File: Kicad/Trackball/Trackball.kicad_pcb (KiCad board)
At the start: 2 copper layers, 231.1 x 134.1 mm, 52 parts, among them J1 Battery, J10 Conn_01x04_Female, J11 Conn_01x04_Female, J12 Conn_01x04_Female, J13 Conn_01x04_Female, J14 Conn_01x04_Female, J15 Conn_01x04_Female, J17 Conn_01x04_Female, J18 Conn_01x03_Pin, J19 Conn_01x03_Pin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

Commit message: B4: PCB outlines defined. To do: correct schematics - swap male/female sockets, move the buttons to appropriate PCBs. Add 44mm base and the bottom cover.
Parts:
- SW1, SW2, SW3: moved to F.Cu
- U1: moved to B.Cu
- moved H3 183.0 mm to (232.6, 101.6)
- moved H6 166.0 mm to (199.6, 82.5)
- moved H7 165.9 mm to (199.5, 120.7)
- moved MX4 149.3 mm to (245.0, 64.4), turned to 0 degrees
- moved MX1 149.2 mm to (245.0, 138.7)
- moved MX3 139.7 mm to (120.4, 139.5), turned to 180 degrees
- moved MX6 139.4 mm to (120.4, 64.4), turned to 0 degrees
- moved MX2 116.9 mm to (139.0, 139.5), turned to 180 degrees
- moved MX5 116.4 mm to (139.0, 64.4), turned to 0 degrees
- moved H4 107.0 mm to (221.6, 82.5)
- moved H5 106.9 mm to (221.5, 120.7)
- moved J17 82.0 mm to (73.9, 97.8)
- moved C1 76.8 mm to (28.4, 177.7)
- moved C2 76.8 mm to (29.5, 183.2)
- moved C3 76.8 mm to (29.3, 187.9)
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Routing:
- net Button4: track 61.0 -> 0.00 mm, vias 1 -> 0
- net Button5: track 60.0 -> 0.00 mm, vias 1 -> 0
- net Button6: track 58.9 -> 0.00 mm
- net MOTION: track 53.1 -> 0.00 mm, vias 1 -> 0
- net Button1: track 53.0 -> 0.00 mm, vias 1 -> 0
- net Button3: track 44.9 -> 0.00 mm
- net NCS: track 42.7 -> 0.00 mm, vias 1 -> 0
- net +3V3: track 40.9 -> 0.00 mm
- net SCLK: track 39.3 -> 0.00 mm
- net Net-(J1-Pin_2): track 39.2 -> 0.00 mm
- net Net-(J13-Pin_3): track 37.4 -> 0.00 mm, vias 1 -> 0
- net Button2: track 37.2 -> 0.00 mm, vias 1 -> 0
- net RST: track 35.9 -> 0.00 mm
- net BTReset: track 35.4 -> 0.00 mm
- net Net-(J10-Pin_3): track 34.0 -> 0.00 mm, vias 1 -> 0
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- removed copper zone on B.Cu, net GND_T
- removed copper zone on F.Cu, net GND_T
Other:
- board size 231.1 x 134.1 mm -> 238.4 x 138 mm
- board text added: "ThumbsUp! Trackball v4 44/52.5mm Ball"
- board text added: "u/ak66666 2025-09-19"
- board text added: "u/ak66666 ThumbsUp! Trackball v4 52.5mm Ball"
- board text removed: "ThumbsUp! Trackball v3"
- board text removed: "u/ak66666 2025-08-30"

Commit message: B4: Base,  Cover, 52.5 mm ball platform ready. TODO: add 44mm platform.
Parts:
- removed H2: MountingHole_Pad, MountingHole:MountingHole_2.5mm_Pad
- removed J11, J14, J17: Conn_01x04_Female, Connector_PinSocket_2.54mm:PinSocket_1x04_P2.54mm_Vertical
- removed J7, J8, J9: Conn_01x04_Male, Connector_PinHeader_2.54mm:PinHeader_1x04_P2.54mm_Vertical
- J1: moved to F.Cu
- J10: renamed from J2; value Conn_01x04_Male -> Conn_01x04_Female; footprint Connector_PinHeader_2.54mm:PinHeader_1x04_P2.54mm_Vertical -> Connector_PinSocket_2.54mm:PinSocket_1x04_P2.54mm_Vertical; moved to F.Cu
- J12: renamed from J5; value Conn_01x04_Male -> Conn_01x04_Female; footprint Connector_PinHeader_2.54mm:PinHeader_1x04_P2.54mm_Vertical -> Connector_PinSocket_2.54mm:PinSocket_1x04_P2.54mm_Vertical; moved to F.Cu
- J13: renamed from J3; value Conn_01x04_Male -> Conn_01x04_Female; footprint Connector_PinHeader_2.54mm:PinHeader_1x04_P2.54mm_Vertical -> Connector_PinSocket_2.54mm:PinSocket_1x04_P2.54mm_Vertical; moved to F.Cu
- J15: renamed from J4; value Conn_01x04_Male -> Conn_01x04_Female; footprint Connector_PinHeader_2.54mm:PinHeader_1x04_P2.54mm_Vertical -> Connector_PinSocket_2.54mm:PinSocket_1x04_P2.54mm_Vertical; moved to F.Cu
- J2: renamed from J10; value Conn_01x04_Female -> Conn_01x04_Male; footprint Connector_PinSocket_2.54mm:PinSocket_1x04_P2.54mm_Vertical -> Connector_PinHeader_2.54mm:PinHeader_1x04_P2.54mm_Vertical; moved to B.Cu
- J3: renamed from J13; value Conn_01x04_Female -> Conn_01x04_Male; footprint Connector_PinSocket_2.54mm:PinSocket_1x04_P2.54mm_Vertical -> Connector_PinHeader_2.54mm:PinHeader_1x04_P2.54mm_Vertical; moved to B.Cu
- J4: renamed from J15; value Conn_01x04_Female -> Conn_01x04_Male; footprint Connector_PinSocket_2.54mm:PinSocket_1x04_P2.54mm_Vertical -> Connector_PinHeader_2.54mm:PinHeader_1x04_P2.54mm_Vertical; moved to B.Cu
- J5: renamed from J12; value Conn_01x04_Female -> Conn_01x04_Male; footprint Connector_PinSocket_2.54mm:PinSocket_1x04_P2.54mm_Vertical -> Connector_PinHeader_2.54mm:PinHeader_1x04_P2.54mm_Vertical; moved to B.Cu
- moved J1 72.8 mm to (140.7, 89.1), turned to -135 degrees
- moved BT_RESET1 37.2 mm to (163.2, 68.1), turned to 90 degrees
- moved STUDIO_UNLOCK1 24.5 mm to (163.2, 135.8)
- moved RESET1 20.8 mm to (153.5, 143.7)
- moved BT_SELECT1 20.6 mm to (153.5, 60.2), turned to 180 degrees
- moved H7 0.38 mm to (199.7, 120.3)
- moved H6 0.21 mm to (199.7, 82.7)
- moved H1 0.20 mm to (188.8, 101.6)
- moved H3 0.20 mm to (232.4, 101.6)
- moved H4 0.18 mm to (221.4, 82.6)
- moved H5 0.15 mm to (221.4, 120.6)
- turned J10 to -45 degrees
- turned J12 to -90 degrees
- turned J13 to -135 degrees
- turned J15 to -90 degrees
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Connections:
- H3 pad 1: GND_T -> GNDA
- H4 pad 1: GND -> GNDA
- H5 pad 1: GND -> GNDA
- H6 pad 1: GND_T -> GNDA
- H7 pad 1: GND_T -> GNDA
- J10 pad 1: unconnected-(J2-Pin_1-Pad1) -> GND
- J10 pad 2: Button2 -> GND
- J10 pad 3: Button3 -> GND
- J10 pad 4: unconnected-(J2-Pin_4-Pad4) -> GND
- J12 pad 4: GND -> Button1
- J13 pad 1: unconnected-(J3-Pin_1-Pad1) -> GND
- J13 pad 2: Button5 -> GND
- J13 pad 3: Button6 -> GND
- J13 pad 4: unconnected-(J3-Pin_4-Pad4) -> GND
- J15 pad 4: GND -> Button4
- J2 pad 1: unconnected-(J10-Pin_1-Pad1) -> GNDA
- J2 pad 2: Net-(J10-Pin_2) -> GNDA
- J2 pad 3: Net-(J10-Pin_3) -> GNDA
- J2 pad 4: unconnected-(J10-Pin_4-Pad4) -> GNDA
- J3 pad 1: unconnected-(J13-Pin_1-Pad1) -> GNDA
- J3 pad 2: Net-(J13-Pin_2) -> GNDA
- J3 pad 3: Net-(J13-Pin_3) -> GNDA
- J3 pad 4: unconnected-(J13-Pin_4-Pad4) -> GNDA
- J4 pad 4: GNDA -> Net-(J4-Pin_4)
- J5 pad 1: GNDA -> Net-(J5-Pin_1)
- J5 pad 2: GNDA -> Net-(J5-Pin_1)
- J5 pad 3: GNDA -> Net-(J5-Pin_1)
- J5 pad 4: GNDA -> Net-(J5-Pin_4)
- MX1 pad 1: Button1 -> Net-(J4-Pin_4)
- MX1 pad 2: GND -> GNDA
- MX2 pad 1: GNDA -> GND
- MX2 pad 2: Net-(J10-Pin_2) -> Button2
- MX3 pad 1: GNDA -> GND
- MX3 pad 2: Net-(J10-Pin_3) -> Button3
- MX4 pad 1: GND -> GNDA
- MX4 pad 2: Button4 -> Net-(J5-Pin_4)
- MX5 pad 1: Net-(J13-Pin_2) -> Button5
- MX5 pad 2: GNDA -> GND
- MX6 pad 1: Net-(J13-Pin_3) -> Button6
- MX6 pad 2: GNDA -> GND
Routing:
- net Button6: track 0.00 -> 66.4 mm, vias 0 -> 2
- net SCLK: track 0.00 -> 65.0 mm, vias 0 -> 1
- net Unlock: track 0.00 -> 59.4 mm, vias 0 -> 1
- net RST: track 0.00 -> 55.2 mm, vias 0 -> 1
- net Button3: track 0.00 -> 52.6 mm, vias 0 -> 2
- net MOTION: track 0.00 -> 52.2 mm, vias 0 -> 1
- net SDIO: track 0.00 -> 49.0 mm, vias 0 -> 1
- net BTSelect: track 0.00 -> 45.8 mm, vias 0 -> 2
- net Net-(J1-Pin_2): track 0.00 -> 44.4 mm, vias 0 -> 1
- net Button5: track 0.00 -> 44.3 mm
- net NCS: track 0.00 -> 40.3 mm, vias 0 -> 1
- net BTReset: track 0.00 -> 39.9 mm, vias 0 -> 1
- net Button4: track 0.00 -> 39.8 mm, vias 0 -> 1
- net +3V3: track 0.00 -> 34.0 mm, vias 0 -> 1
- net Button1: track 0.00 -> 32.9 mm, vias 0 -> 1
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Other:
- board size 238.4 x 138 mm -> 278.5 x 138.1 mm
- board text added: "BT CLEAR"
- board text added: "CONTROL FINGER-THUMB"
- board text added: "HAND RIGHT-LEFT"
- board text added: "ProMicro on the other side FACE DOWN"
- board text added: "ZMK.STUDIO UNLOCK"
- board text added: "u/ak66666 ThumbsUp! Trackball v4 2025-09-19"
- board text removed: "BT RESET"
- board text removed: "ThumbsUp! Trackball v4 44/52.5mm Ball"
- board text removed: "u/ak66666 2025-09-19"

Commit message: B4: Added 44mm platform. TODO: Prepare Gerbers for fabrication.
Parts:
- added H1: MountingHole_Pad, MountingHole:MountingHole_2.5mm_Pad, F.Cu at (322.7, 101.6)
- added H3: MountingHole_Pad, MountingHole:MountingHole_2.5mm_Pad, F.Cu at (362.1, 101.7)
- added H4: MountingHole_Pad, MountingHole:MountingHole_2.5mm_Pad, F.Cu at (352.2, 84.5)
- added H5: MountingHole_Pad, MountingHole:MountingHole_2.5mm_Pad, F.Cu at (352.2, 118.8)
- added H6: MountingHole_Pad, MountingHole:MountingHole_2.5mm_Pad, F.Cu at (332.5, 84.5)
- added H7: MountingHole_Pad, MountingHole:MountingHole_2.5mm_Pad, F.Cu at (332.4, 118.7)
- added J2: Conn_01x04_Male, Connector_PinHeader_2.54mm:PinHeader_1x04_P2.54mm_Vertical, B.Cu at (324.6, 80.4)
- added J3: Conn_01x04_Male, Connector_PinHeader_2.54mm:PinHeader_1x04_P2.54mm_Vertical, B.Cu at (324.6, 122.8)
- added J4: Conn_01x04_Male, Connector_PinHeader_2.54mm:PinHeader_1x04_P2.54mm_Vertical, B.Cu at (385.6, 126.0)
- added J5: Conn_01x04_Male, Connector_PinHeader_2.54mm:PinHeader_1x04_P2.54mm_Vertical, B.Cu at (385.6, 77.2)
- added MX1: MX-NoLED, keyswitches.pretty-master:Kailh_socket_PG1350, F.Cu at (376.8, 138.7)
- added MX4: MX-NoLED, keyswitches.pretty-master:Kailh_socket_PG1350, F.Cu at (376.8, 64.4)
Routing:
- net Net-(J5-Pin_4): track 15.5 -> 31.0 mm
- net Net-(J4-Pin_4): track 10.0 -> 20.0 mm
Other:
- board size 278.5 x 138.1 mm -> 410.3 x 138.1 mm
- board text added: "u/ak66666 ThumbsUp! Trackball v4 44mm Ball"

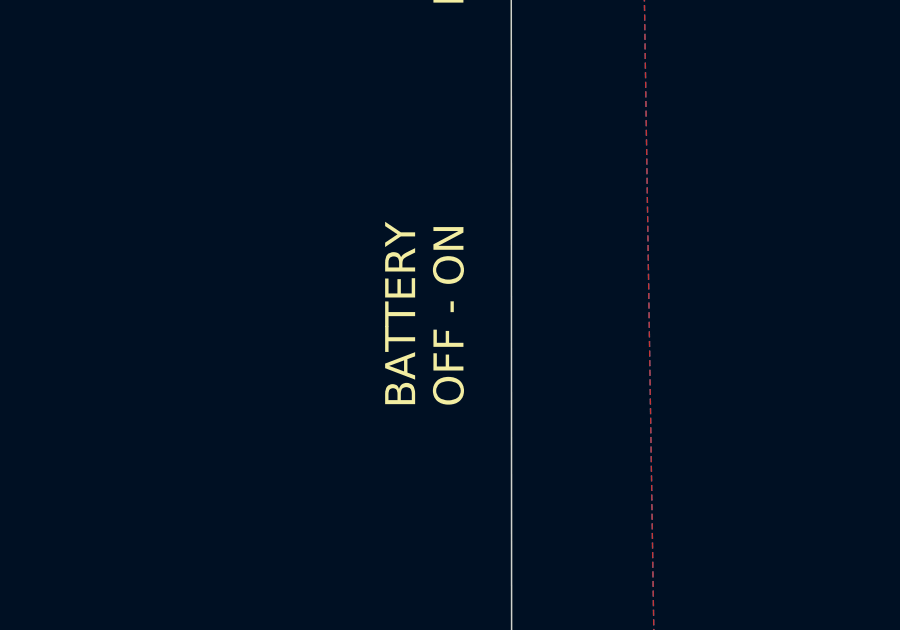
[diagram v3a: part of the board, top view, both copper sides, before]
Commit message: B4: Corrected labels on the protective cover. TODO: Prepare Gerbers for fabrication.
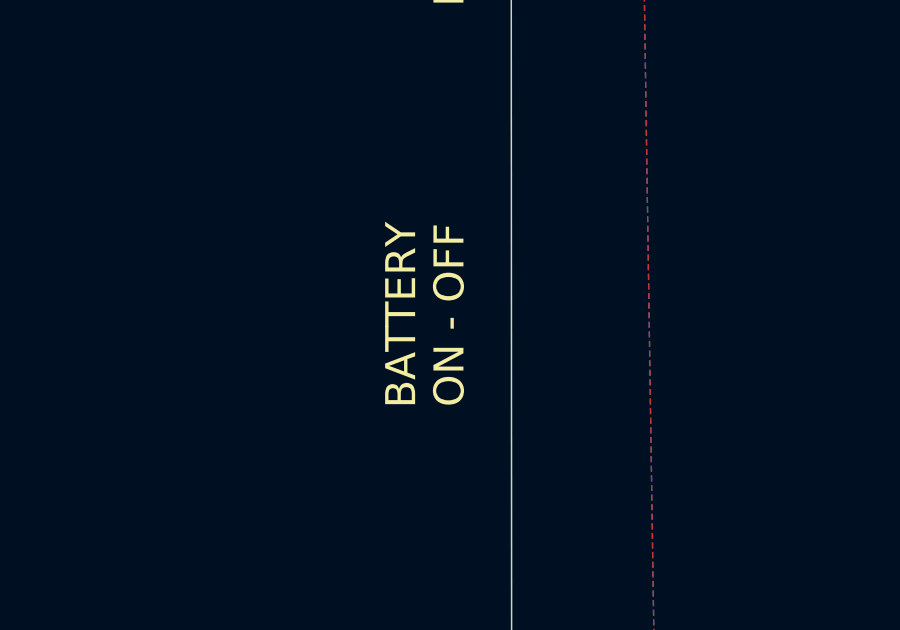
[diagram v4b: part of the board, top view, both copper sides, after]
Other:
- board text added: "BATTERY ON - OFF"

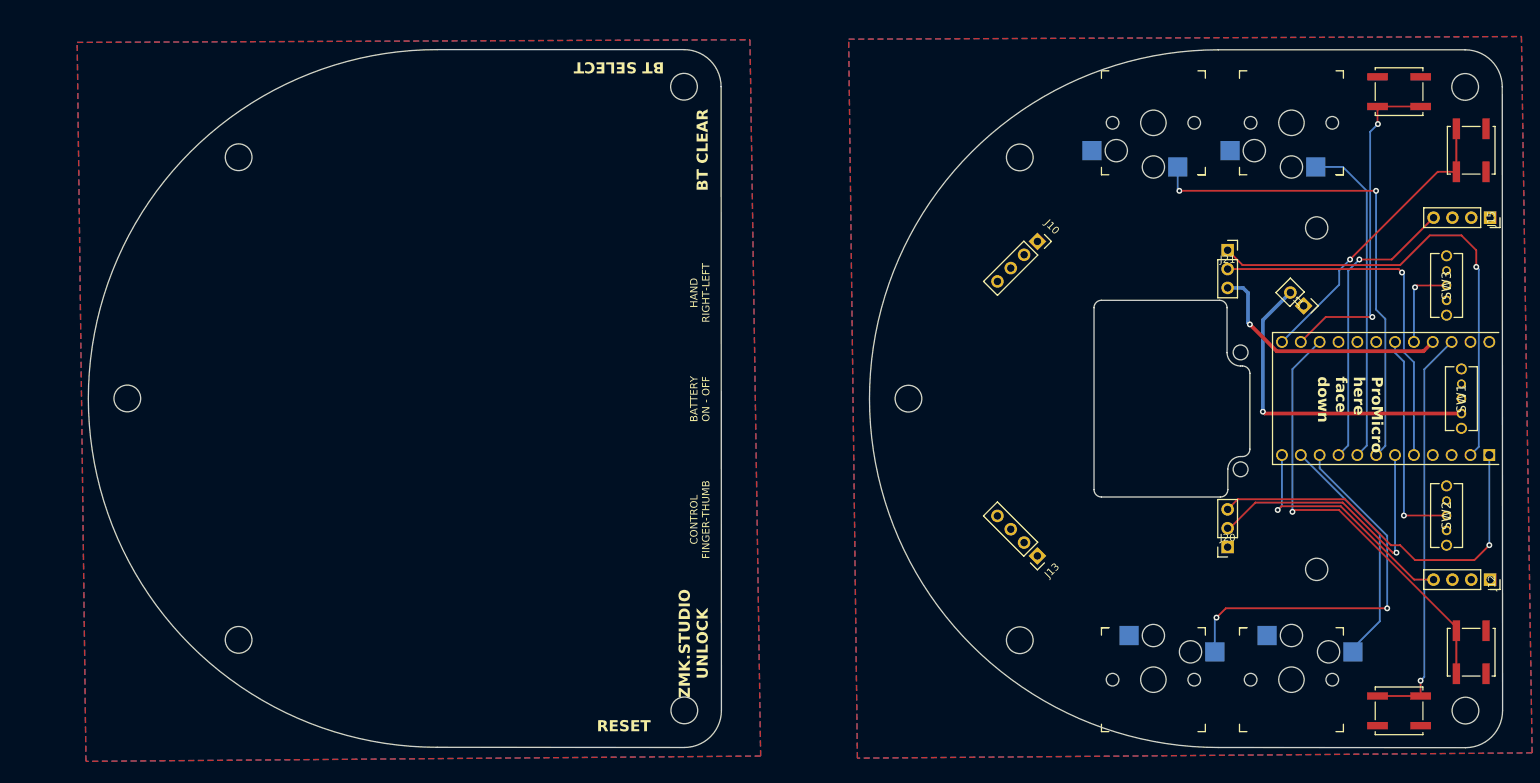
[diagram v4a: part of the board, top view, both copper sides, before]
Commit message: B4: Trying to hoax JLC to think the bottom plate is small - added pad holes instead of simple holes.
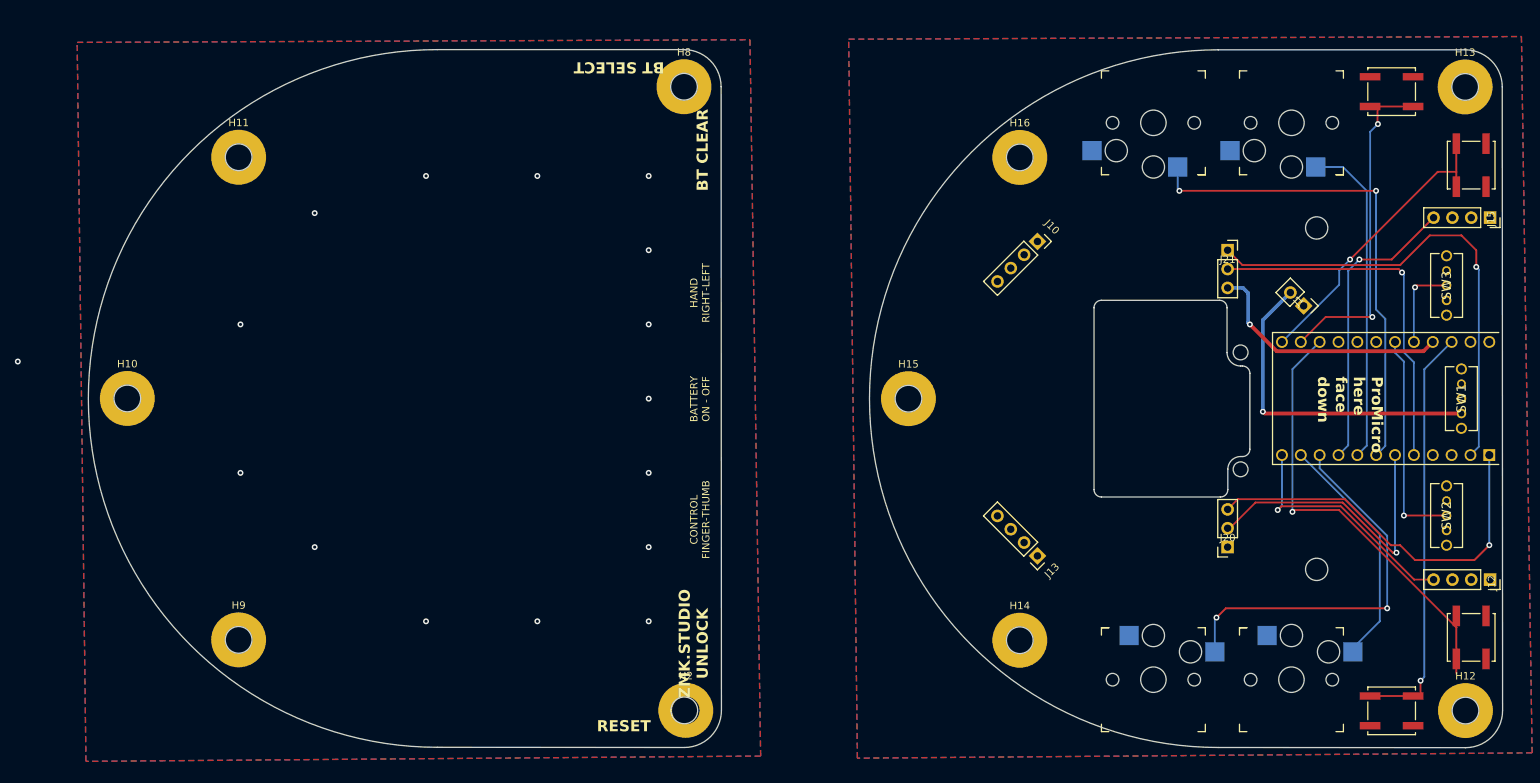
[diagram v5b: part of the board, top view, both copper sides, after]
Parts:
- added H10: MountingHole_Pad, MountingHole:MountingHole_3.7mm_Pad, F.Cu at (-17.8, 101.6)
- added H11: MountingHole_Pad, MountingHole:MountingHole_3.7mm_Pad, F.Cu at (-2.85, 69.1)
- added H12: MountingHole_Pad, MountingHole:MountingHole_3.7mm_Pad, F.Cu at (162.4, 143.6)
- added H13: MountingHole_Pad, MountingHole:MountingHole_3.7mm_Pad, F.Cu at (162.4, 59.6)
- added H14: MountingHole_Pad, MountingHole:MountingHole_3.7mm_Pad, F.Cu at (102.4, 134.2)
- added H15: MountingHole_Pad, MountingHole:MountingHole_3.7mm_Pad, F.Cu at (87.4, 101.6)
- added H16: MountingHole_Pad, MountingHole:MountingHole_3.7mm_Pad, F.Cu at (102.4, 69.1)
- added H2: MountingHole_Pad, MountingHole:MountingHole_3.7mm_Pad, F.Cu at (57.4, 143.6)
- added H8: MountingHole_Pad, MountingHole:MountingHole_3.7mm_Pad, F.Cu at (57.2, 59.6)
- added H9: MountingHole_Pad, MountingHole:MountingHole_3.7mm_Pad, F.Cu at (-2.85, 134.1)
- moved BT_RESET1 2.00 mm to (163.2, 70.1)
- moved STUDIO_UNLOCK1 2.00 mm to (163.2, 133.8)
- moved BT_SELECT1 1.00 mm to (152.5, 60.2)
- moved RESET1 1.00 mm to (152.5, 143.7)
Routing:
- net Unlock: track 59.4 -> 60.9 mm
- net GND: vias 0 -> 9
- net (no net): vias 0 -> 7
- added copper zone on B.Cu, net GNDB
- added copper zone on F.Cu, net GNDB
